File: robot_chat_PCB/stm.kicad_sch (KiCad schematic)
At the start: 24 parts, among them J201 Conn_02x07_Odd_Even, SW201 SW_Push, U201 STM32G070RBTx, Y201 16MHz

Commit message: Mise à jour placement
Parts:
- C203, C204, C206, C207: footprint Capacitor_SMD:C_0603_1608Metric -> Capacitor_SMD:C_0402_1005Metric
- CS201: value TestPoint -> CS
- J201: value Conn_02x07_Odd_Even -> STLink
- LIDAR_RX201: value TestPoint -> L-RX
- LIDAR_TX201: value TestPoint -> L-TX
- SDI201: value TestPoint -> MOSI
- SDO201: value TestPoint -> MISO
- SPI_CLK201: value TestPoint -> SPI_CLK
- SW201: value SW_Push -> RST
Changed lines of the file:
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@@
       (effects (font (size 1.27 1.27)))
     )
-    (property "Footprint" "Capacitor_SMD:C_0603_1608Metric" (at 76.2 49.53 0)
+    (property "Footprint" "Capacitor_SMD:C_0402_1005Metric" (at 76.2 49.53 0)
       (effects (font (size 1.27 1.27)) hide)
     )
@@
     (in_bom yes) (on_board yes) (dnp no)
     (property "Reference" "SDO201" (at 195.58 118.11 90)
-      (effects (font (size 1.27 1.27)))
-    )
-    (property "Value" "TestPoint" (at 199.898 115.57 0)
-      (effects (font (size 1.27 1.27)) (justify left) hide)
+      (effects (font (size 1.27 1.27)) hide)
+    )
+    (property "Value" "MISO" (at 196.85 118.11 90)
+      (effects (font (size 1.27 1.27)) (justify left))
     )
     (property "Footprint" "TestPoint:TestPoint_Pad_D1.0mm" (at 201.93 113.03 0)
@@
     (in_bom yes) (on_board yes) (dnp no) (fields_autoplaced)
     (property "Reference" "J201" (at 234.95 24.13 0)
-      (effects (font (size 1.27 1.27)))
-    )
-    (property "Value" "Conn_02x07_Odd_Even" (at 234.95 26.67 0)
+      (effects (font (size 1.27 1.27)) hide)
+    )
+    (property "Value" "STLink" (at 234.95 26.67 0)
       (effects (font (size 1.27 1.27)))
     )
@@
       (effects (font (size 1.27 1.27)) (justify left))
     )
-    (property "Footprint" "Capacitor_SMD:C_0603_1608Metric" (at 115.57 57.15 0)
+    (property "Footprint" "Capacitor_SMD:C_0402_1005Metric" (at 115.57 57.15 0)
       (effects (font (size 1.27 1.27)) hide)
     )
@@
     (in_bom yes) (on_board yes) (dnp no)
     (property "Reference" "LIDAR_RX201" (at 193.04 140.97 90)
-      (effects (font (size 1.27 1.27)))
-    )
-    (property "Value" "TestPoint" (at 199.898 138.43 0)
-      (effects (font (size 1.27 1.27)) (justify left) hide)
+      (effects (font (size 1.27 1.27)) hide)
+    )
+    (property "Value" "L-RX" (at 196.85 140.97 90)
+      (effects (font (size 1.27 1.27)) (justify left))
     )
     (property "Footprint" "TestPoint:TestPoint_Pad_D1.0mm" (at 201.93 135.89 0)
@@
     (in_bom yes) (on_board yes) (dnp no)
     (property "Reference" "SPI_CLK201" (at 193.04 129.54 90)
-      (effects (font (size 1.27 1.27)))
-    )
-    (property "Value" "TestPoint" (at 199.898 127 0)
-      (effects (font (size 1.27 1.27)) (justify left) hide)
+      (effects (font (size 1.27 1.27)) hide)
+    )
+    (property "Value" "SPI_CLK" (at 196.85 129.54 90)
+      (effects (font (size 1.27 1.27)) (justify left))
     )
     (property "Footprint" "TestPoint:TestPoint_Pad_D1.0mm" (at 201.93 124.46 0)
@@
     (in_bom yes) (on_board yes) (dnp no)
     (property "Reference" "SDI201" (at 195.58 113.03 90)
-      (effects (font (size 1.27 1.27)))
-    )
-    (property "Value" "TestPoint" (at 199.898 110.49 0)
-      (effects (font (size 1.27 1.27)) (justify left) hide)
+      (effects (font (size 1.27 1.27)) hide)
+    )
+    (property "Value" "MOSI" (at 196.85 113.03 90)
+      (effects (font (size 1.27 1.27)) (justify left))
     )
     (property "Footprint" "TestPoint:TestPoint_Pad_D1.0mm" (at 201.93 107.95 0)
@@
     (in_bom yes) (on_board yes) (dnp no)
     (property "Reference" "CS201" (at 195.58 123.19 90)
-      (effects (font (size 1.27 1.27)))
-    )
-    (property "Value" "TestPoint" (at 199.898 120.65 0)
-      (effects (font (size 1.27 1.27)) (justify left) hide)
+      (effects (font (size 1.27 1.27)) hide)
+    )
+    (property "Value" "CS" (at 196.85 123.19 90)
+      (effects (font (size 1.27 1.27)) (justify left))
     )
     (property "Footprint" "TestPoint:TestPoint_Pad_D1.0mm" (at 201.93 118.11 0)
@@
     (in_bom yes) (on_board yes) (dnp no)
     (property "Reference" "LIDAR_TX201" (at 193.04 135.89 90)
-      (effects (font (size 1.27 1.27)))
-    )
-    (property "Value" "TestPoint" (at 199.898 133.35 0)
-      (effects (font (size 1.27 1.27)) (justify left) hide)
+      (effects (font (size 1.27 1.27)) hide)
+    )
+    (property "Value" "L-TX" (at 196.85 135.89 90)
+      (effects (font (size 1.27 1.27)) (justify left))
     )
     (property "Footprint" "TestPoint:TestPoint_Pad_D1.0mm" (at 201.93 130.81 0)
@@
     (in_bom yes) (on_board yes) (dnp no) (fields_autoplaced)
     (property "Reference" "SW201" (at 77.47 53.34 0)
-      (effects (font (size 1.27 1.27)))
-    )
-    (property "Value" "SW_Push" (at 77.47 55.88 0)
+      (effects (font (size 1.27 1.27)) hide)
+    )
+    (property "Value" "RST" (at 77.47 55.88 0)
       (effects (font (size 1.27 1.27)))
     )
@@
       (effects (font (size 1.27 1.27)) (justify left))
     )
-    (property "Footprint" "Capacitor_SMD:C_0603_1608Metric" (at 127 57.15 0)
+    (property "Footprint" "Capacitor_SMD:C_0402_1005Metric" (at 127 57.15 0)
       (effects (font (size 1.27 1.27)) hide)
     )
@@
       (effects (font (size 1.27 1.27)))
     )
-    (property "Footprint" "Capacitor_SMD:C_0603_1608Metric" (at 73.66 74.93 0)
-      (effects (font (size 1.27 1.27)) hide)
-    )
+    (property "Footprint" "Capacitor_SMD:C_0402_1005Metric" (at 73.66 74.93 0)
+      (effects (font (size 1.27 1.27)) hide)
+    )

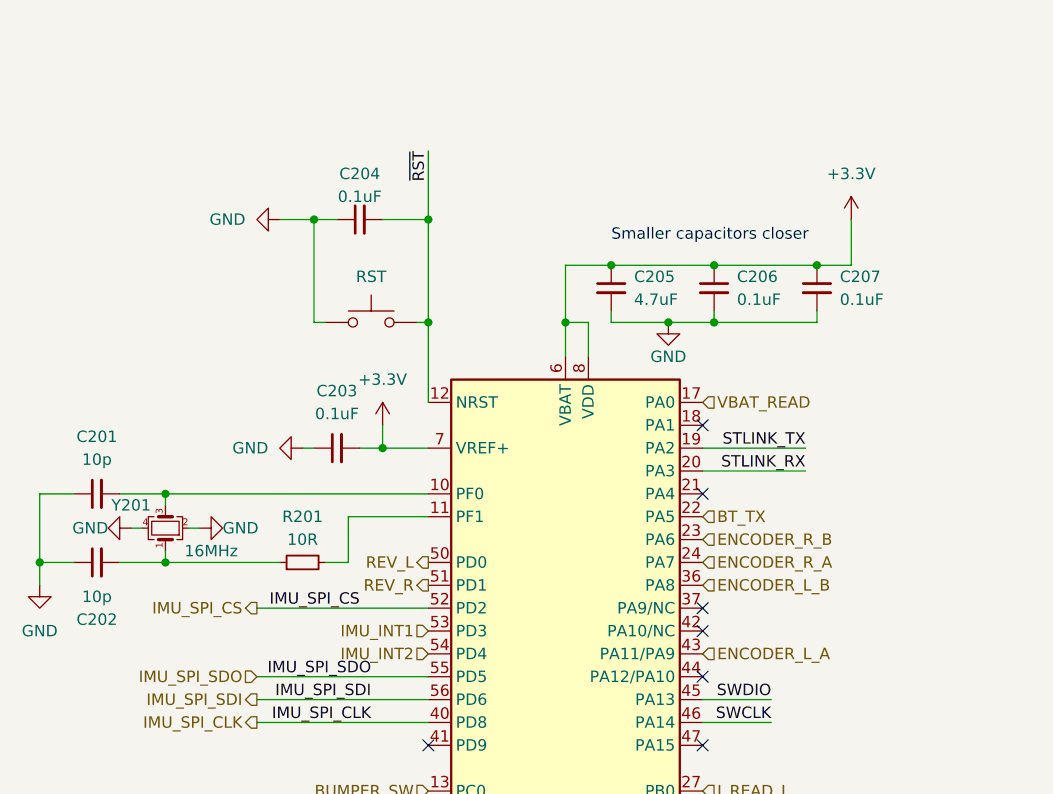
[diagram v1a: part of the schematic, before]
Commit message: changed Rsense position
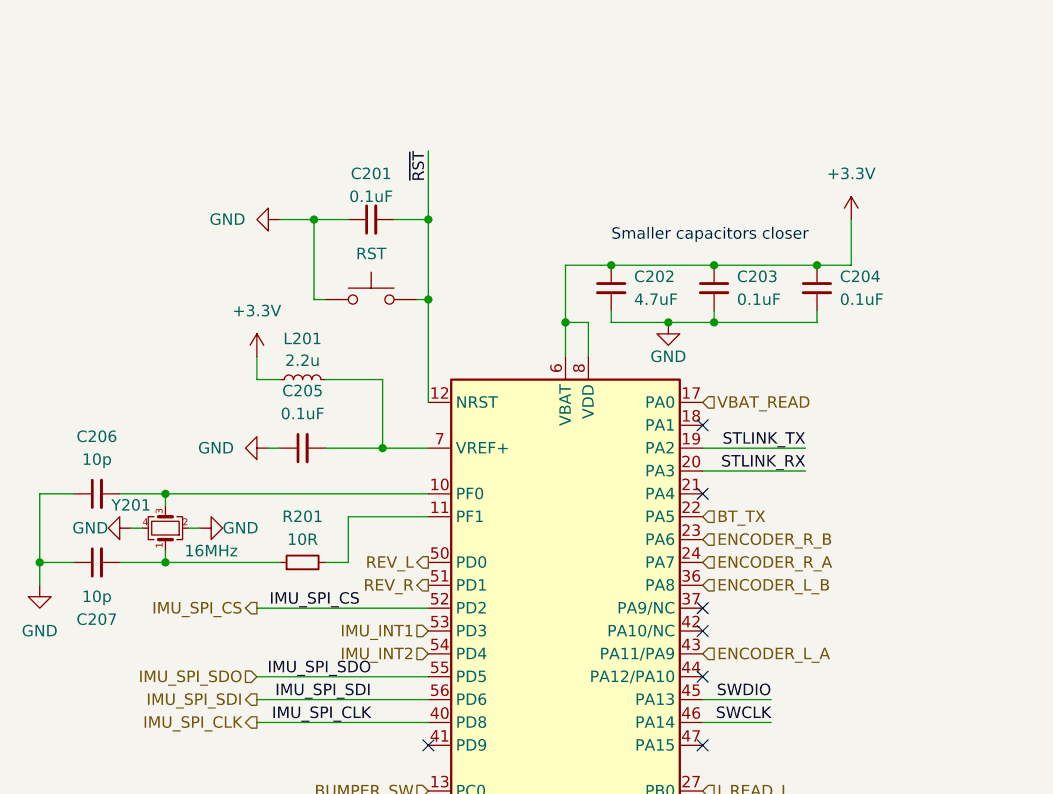
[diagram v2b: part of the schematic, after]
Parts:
- added L201: 2.2u, Inductor_SMD:L_0603_1608Metric, symbol Device:L_Small
- renumbered C204 to C201, C205 to C202, C206 to C203, C207 to C204, C203 to C205, C201 to C206, C202 to C207
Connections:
- net +3.3V: now also L201.1; no longer C205.2, U201.7 (VREF+)
- new net: C205.2, L201.2, U201.7 (VREF+)
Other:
- moved on the sheet: C201, C205

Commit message: Routage
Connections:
- net IMU_SPI_CLK: now also U201.57 (PB3); no longer U201.40 (PD8)
- net IMU_SPI_CS: now also U201.58 (PB4); no longer U201.52 (PD2)
- net I_READ_L: now also U201.30 (PB10); no longer U201.27 (PB0)
- net LIDAR_RX: now also U201.25 (PC4); no longer U201.26 (PC5)
- net LIDAR_TX: now also U201.26 (PC5); no longer U201.25 (PC4)
- net USER_LED_0: now also U201.60 (PB6); no longer U201.58 (PB4)
- net USER_LED_1: now also U201.61 (PB7); no longer U201.59 (PB5)
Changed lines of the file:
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@@
   (junction (at 54.61 87.63) (diameter 0) (color 0 0 0 0)
   )
-  (no_connect (at 114.3 130.81))
-  (no_connect (at 114.3 118.11))
+  (no_connect (at 114.3 125.73))
+  (no_connect (at 114.3 140.97))
   (no_connect (at 83.82 107.95))
   (no_connect (at 241.3 30.48))
-  (no_connect (at 114.3 128.27))
+  (no_connect (at 83.82 92.71))
   (no_connect (at 241.3 40.64))
   (no_connect (at 114.3 107.95))
@@
   (no_connect (at 83.82 133.35))
   (no_connect (at 114.3 80.01))
+  (no_connect (at 83.82 105.41))
   (no_connect (at 114.3 143.51))
-  (no_connect (at 114.3 138.43))
+  (no_connect (at 114.3 113.03))
   (no_connect (at 114.3 146.05))
   (no_connect (at 114.3 100.33))
   (no_connect (at 83.82 135.89))
   (no_connect (at 83.82 151.13))
-  (no_connect (at 114.3 140.97))
-  (no_connect (at 114.3 120.65))
+  (no_connect (at 114.3 118.11))
   (no_connect (at 241.3 38.1))
   (no_connect (at 114.3 72.39))
@@
     (stroke (width 0) (type default))
   )
-  (wire (pts (xy 64.77 105.41) (xy 83.82 105.41))
-    (stroke (width 0) (type default))
-  )
   (polyline (pts (xy 176.53 81.28) (xy 176.53 165.1))
     (stroke (width 0) (type dash))
@@
     (stroke (width 0) (type default))
   )
+  (wire (pts (xy 114.3 123.19) (xy 129.54 123.19))
+    (stroke (width 0) (type default))
+  )
   (wire (pts (xy 99.06 54.61) (xy 104.14 54.61))
     (stroke (width 0) (type default))
@@
   )
   (wire (pts (xy 220.98 33.02) (xy 228.6 33.02))
+    (stroke (width 0) (type default))
+  )
+  (wire (pts (xy 114.3 120.65) (xy 129.54 120.65))
     (stroke (width 0) (type default))
   )
@@
   )
   (wire (pts (xy 83.82 41.91) (xy 83.82 49.53))
-    (stroke (width 0) (type default))
-  )
-  (wire (pts (xy 64.77 92.71) (xy 83.82 92.71))
     (stroke (width 0) (type default))
   )
@@
     (effects (font (size 1.27 1.27)) (justify left bottom))
   )
-  (label "IMU_SPI_CLK" (at 77.47 105.41 180) (fields_autoplaced)
-    (effects (font (size 1.27 1.27)) (justify right bottom))
-  )
-  (label "LIDAR_TX" (at 81.28 123.19 180) (fields_autoplaced)
+  (label "IMU_SPI_CLK" (at 116.84 120.65 0) (fields_autoplaced)
+    (effects (font (size 1.27 1.27)) (justify left bottom))
+  )
+  (label "LIDAR_TX" (at 80.01 125.73 180) (fields_autoplaced)
     (effects (font (size 1.27 1.27)) (justify right bottom))
   )
@@
     (effects (font (size 1.27 1.27)) (justify right bottom))
   )
-  (label "IMU_SPI_CS" (at 76.2 92.71 180) (fields_autoplaced)
-    (effects (font (size 1.27 1.27)) (justify right bottom))
+  (label "IMU_SPI_CS" (at 118.11 123.19 0) (fields_autoplaced)
+    (effects (font (size 1.27 1.27)) (justify left bottom))
   )
   (label "STLINK_TX" (at 125.73 74.93 180) (fields_autoplaced)
@@
     (effects (font (size 1.27 1.27)) (justify right bottom))
   )
-  (label "LIDAR_RX" (at 81.28 125.73 180) (fields_autoplaced)
+  (label "LIDAR_RX" (at 80.01 123.19 180) (fields_autoplaced)
     (effects (font (size 1.27 1.27)) (justify right bottom))
   )
@@
     (effects (font (size 1.27 1.27)) (justify right bottom))
   )
-  (global_label "USER_LED_0" (shape input) (at 114.3 123.19 0) (fields_autoplaced)
-    (effects (font (size 1.27 1.27)) (justify left))
-    (property "Intersheetrefs" "${INTERSHEET_REFS}" (at 128.836 123.19 0)
+  (global_label "USER_LED_0" (shape input) (at 114.3 128.27 0) (fields_autoplaced)
+    (effects (font (size 1.27 1.27)) (justify left))
+    (property "Intersheetrefs" "${INTERSHEET_REFS}" (at 128.836 128.27 0)
       (effects (font (size 1.27 1.27)) (justify left) hide)
     )
@@
     )
   )
-  (global_label "USER_LED_1" (shape input) (at 114.3 125.73 0) (fields_autoplaced)
-    (effects (font (size 1.27 1.27)) (justify left))
-    (property "Intersheetrefs" "${INTERSHEET_REFS}" (at 128.836 125.73 0)
+  (global_label "USER_LED_1" (shape input) (at 114.3 130.81 0) (fields_autoplaced)
+    (effects (font (size 1.27 1.27)) (justify left))
+    (property "Intersheetrefs" "${INTERSHEET_REFS}" (at 128.836 130.81 0)
       (effects (font (size 1.27 1.27)) (justify left) hide)
     )
@@
     (effects (font (size 1.27 1.27)) (justify left))
   )
-  (hierarchical_label "LIDAR_TX" (shape input) (at 71.12 123.19 180) (fields_autoplaced)
+  (hierarchical_label "LIDAR_TX" (shape input) (at 71.12 125.73 180) (fields_autoplaced)
     (effects (font (size 1.27 1.27)) (justify right))
   )
@@
     (effects (font (size 1.27 1.27)) (justify left))
   )
-  (hierarchical_label "IMU_SPI_CLK" (shape output) (at 64.77 105.41 180) (fields_autoplaced)
-    (effects (font (size 1.27 1.27)) (justify right))
+  (hierarchical_label "IMU_SPI_CLK" (shape output) (at 129.54 120.65 0) (fields_autoplaced)
+    (effects (font (size 1.27 1.27)) (justify left))
   )
   (hierarchical_label "LIDAR_SPEED" (shape output) (at 114.3 151.13 0) (fields_autoplaced)
@@
     (effects (font (size 1.27 1.27)) (justify left))
   )
-  (hierarchical_label "IMU_SPI_CS" (shape output) (at 64.77 92.71 180) (fields_autoplaced)
-    (effects (font (size 1.27 1.27)) (justify right))
+  (hierarchical_label "IMU_SPI_CS" (shape output) (at 129.54 123.19 0) (fields_autoplaced)
+    (effects (font (size 1.27 1.27)) (justify left))
   )
   (hierarchical_label "REV_R" (shape output) (at 83.82 90.17 180) (fields_autoplaced)
@@
     (effects (font (size 1.27 1.27)) (justify left))
   )
-  (hierarchical_label "I_READ_L" (shape input) (at 114.3 113.03 0) (fields_autoplaced)
+  (hierarchical_label "I_READ_L" (shape input) (at 114.3 138.43 0) (fields_autoplaced)
     (effects (font (size 1.27 1.27)) (justify left))
   )
@@
     (effects (font (size 1.27 1.27)) (justify right))
   )
-  (hierarchical_label "LIDAR_RX" (shape output) (at 71.12 125.73 180) (fields_autoplaced)
-    (effects (font (size 1.27 1.27)) (justify right))
-  )
+  (hierarchical_label "LIDAR_RX" (shape output) (at 71.12 123.19 180) (fields_autoplaced)
+    (effects (font (size 1.27 1.27)) (justify right))
+  )

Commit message: routage final v1.1
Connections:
- net ENCODER_L_A: now also U201.37 (PA9/NC); no longer U201.43 (PA11/PA9)
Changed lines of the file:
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@@
   (no_connect (at 114.3 95.25))
   (no_connect (at 83.82 120.65))
-  (no_connect (at 114.3 92.71))
   (no_connect (at 83.82 133.35))
   (no_connect (at 114.3 80.01))
   (no_connect (at 83.82 105.41))
+  (no_connect (at 114.3 97.79))
   (no_connect (at 114.3 143.51))
   (no_connect (at 114.3 113.03))
@@
     (effects (font (size 1.27 1.27)) (justify right))
   )
-  (hierarchical_label "ENCODER_L_A" (shape input) (at 114.3 97.79 0) (fields_autoplaced)
-    (effects (font (size 1.27 1.27)) (justify left))
-  )
+  (hierarchical_label "ENCODER_L_A" (shape input) (at 114.3 92.71 0) (fields_autoplaced)
+    (effects (font (size 1.27 1.27)) (justify left))
+  )

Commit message: Routage final v1.2
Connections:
- net QUARTZ_0: now reaches C206.2, U201.10 (PF0), Y201.3
- net QUARTZ_1: now reaches R201.2, U201.11 (PF1)
- net VREF+: now reaches C205.2, L201.2, U201.7 (VREF+)
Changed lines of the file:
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@@
   (junction (at 115.57 60.96) (diameter 0) (color 0 0 0 0)
   )
-  (junction (at 78.74 74.93) (diameter 0) (color 0 0 0 0)
-  )
   (junction (at 224.79 85.09) (diameter 0) (color 0 0 0 0)
   )
@@
   )
   (junction (at 54.61 80.01) (diameter 0) (color 0 0 0 0)
+  )
+  (junction (at 80.01 74.93) (diameter 0) (color 0 0 0 0)
   )
   (junction (at 229.87 85.09) (diameter 0) (color 0 0 0 0)
@@
     (stroke (width 0) (type default))
   )
-  (wire (pts (xy 78.74 67.31) (xy 78.74 74.93))
+  (wire (pts (xy 80.01 67.31) (xy 80.01 74.93))
     (stroke (width 0) (type default))
   )
@@
     (stroke (width 0) (type default))
   )
-  (wire (pts (xy 72.39 87.63) (xy 74.93 87.63))
+  (wire (pts (xy 72.39 87.63) (xy 73.66 87.63))
     (stroke (width 0) (type default))
   )
@@
     (stroke (width 0) (type default))
   )
-  (wire (pts (xy 78.74 74.93) (xy 83.82 74.93))
+  (wire (pts (xy 72.39 74.93) (xy 80.01 74.93))
     (stroke (width 0) (type default))
   )
@@
     (stroke (width 0) (type dash))
   )
+  (wire (pts (xy 80.01 74.93) (xy 83.82 74.93))
+    (stroke (width 0) (type default))
+  )
   (polyline (pts (xy 176.53 12.7) (xy 176.53 81.28))
     (stroke (width 0) (type dash))
@@
     (stroke (width 0) (type default))
   )
-  (wire (pts (xy 78.74 67.31) (xy 72.39 67.31))
+  (wire (pts (xy 80.01 67.31) (xy 72.39 67.31))
     (stroke (width 0) (type default))
   )
@@
     (stroke (width 0) (type default))
   )
-  (wire (pts (xy 74.93 87.63) (xy 74.93 82.55))
+  (wire (pts (xy 73.66 87.63) (xy 73.66 82.55))
     (stroke (width 0) (type default))
   )
@@
     (stroke (width 0) (type default))
   )
-  (wire (pts (xy 74.93 82.55) (xy 83.82 82.55))
+  (wire (pts (xy 73.66 82.55) (xy 83.82 82.55))
     (stroke (width 0) (type default))
   )
@@
   )
   (wire (pts (xy 49.53 87.63) (xy 54.61 87.63))
-    (stroke (width 0) (type default))
-  )
-  (wire (pts (xy 72.39 74.93) (xy 78.74 74.93))
     (stroke (width 0) (type default))
   )
@@
     (effects (font (size 1.27 1.27)) (justify right bottom))
   )
+  (label "QUARTZ_1" (at 73.66 82.55 0) (fields_autoplaced)
+    (effects (font (size 1.27 1.27)) (justify left bottom))
+  )
   (label "SWCLK" (at 224.79 64.77 270) (fields_autoplaced)
     (effects (font (size 1.27 1.27)) (justify right bottom))
@@
     (effects (font (size 1.27 1.27)) (justify right bottom))
   )
+  (label "VREF+" (at 73.66 67.31 0) (fields_autoplaced)
+    (effects (font (size 1.27 1.27)) (justify left bottom))
+  )
+  (label "QUARTZ_0" (at 63.5 80.01 0) (fields_autoplaced)
+    (effects (font (size 1.27 1.27)) (justify left bottom))
+  )
   (label "SWDIO" (at 121.92 102.87 180) (fields_autoplaced)

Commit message: fixed DRC, added html bom
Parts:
- D1: Farnell Part Number (none) -> 3702487RL
- L201: Farnell Part Number (none) -> 3666006
- SW201: Farnell Part Number (none) -> 1333652
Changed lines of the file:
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@@
+      (effects (font (size 1.27 1.27)) hide)
+    )
+    (property "Farnell Part Number" "3702487RL" (at 201.93 74.93 90)
       (effects (font (size 1.27 1.27)) hide)
     )
@@
     )
     (property "Datasheet" "" (at 213.36 73.66 0)
+      (effects (font (size 1.27 1.27)) hide)
+    )
+    (property "Farnell Part Number" "3702487RL" (at 213.36 74.93 90)
       (effects (font (size 1.27 1.27)) hide)
     )
@@
       (effects (font (size 1.27 1.27)) hide)
     )
+    (property "Farnell Part Number" "3702487RL" (at 224.79 74.93 90)
+      (effects (font (size 1.27 1.27)) hide)
+    )
     (pin "1")
     (pin "2")
@@
       (effects (font (size 1.27 1.27)) hide)
     )
+    (property "Farnell Part Number" "3702487RL" (at 247.65 74.93 90)
+      (effects (font (size 1.27 1.27)) hide)
+    )
     (pin "1")
     (pin "2")
@@
       (effects (font (size 1.27 1.27)) hide)
     )
+    (property "Farnell Part Number" "3702487RL" (at 257.81 74.93 90)
+      (effects (font (size 1.27 1.27)) hide)
+    )
     (pin "1")
     (pin "2")
@@
       (effects (font (size 1.27 1.27)) hide)
     )
+    (property "Farnell Part Number" "3666006" (at 69.85 67.31 90)
+      (effects (font (size 1.27 1.27)) hide)
+    )
     (pin "1")
     (pin "2")
@@
       (effects (font (size 1.27 1.27)) hide)
     )
+    (property "Farnell Part Number" "1333652" (at 77.47 58.42 0)
+      (effects (font (size 1.27 1.27)) hide)
+    )
     (pin "1")
     (pin "2")
@@
       (effects (font (size 1.27 1.27)) hide)
     )
+    (property "Farnell Part Number" "3702487RL" (at 236.22 74.93 90)
+      (effects (font (size 1.27 1.27)) hide)
+    )
